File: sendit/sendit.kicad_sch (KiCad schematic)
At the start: 1 part, among them U2 Seeed_Studio_XIAO_ESP32C6

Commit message: big update on the potential design.
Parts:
- removed U2: Seeed_Studio_XIAO_ESP32C6, Seeed Studio XIAO Series Library:XIAO-Generic-Hybrid-14P-2.54-21X17.8MM, symbol yarrboard:Seeed_Studio_XIAO_ESP32C6
- added R3: 10K, Resistor_SMD:R_1206_3216Metric_Pad1.30x1.75mm_HandSolder, symbol Device:R_Small_US
- added U1: ~, yarrboard:Waveshare-ESP32-S3-dev-kit-SMD, symbol yarrboard:ESP32-S3-DevKitC-1
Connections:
- net GND: now also U1.22 (GND), U1.23 (GND), U1.24 (GND), U1.44 (GND)
- net SCL: now also U1.15 (GPIO9)
- net SDA: now also U1.12 (GPIO8)
- new net +3.3V: R3.2, U1.1 (3V3), U1.2 (3V3)
- new net CH1_A0: U1.40 (GPIO2)
- new net CH1_A1: U1.39 (GPIO42)
- new net CH2_A0: U1.38 (GPIO41)
- new net CH2_A1: U1.37 (GPIO40)
- new net CH3_A0: U1.36 (GPIO39)
- new net CH3_A1: U1.34 (GPIO37)
- new net CH4_A0: U1.33 (GPIO36)
- new net CH4_A1: U1.29 (GPIO48)
- new net CH5_A0: U1.28 (GPIO47)
- new net CH5_A1: U1.27 (GPIO21)
- new net CH6_A0: U1.10 (GPIO17)
- new net CH6_A1: U1.9 (GPIO16)
- new net CH7_A0: U1.8 (GPIO15)
- new net CH7_A1: U1.7 (GPIO7)
- new net CH8_A0: U1.6 (GPIO6)
- new net CH8_A1: U1.5 (GPIO5)
- new net CLK: U1.20 (GPIO14)
- new net MISO: U1.19 (GPIO13)
- new net MOSI: U1.18 (GPIO12)
- new net MUX_ENABLE: R3.1, U1.41 (GPIO1)
- new net SD_CS: U1.17 (GPIO11)
- new net SD_DETECT: U1.16 (GPIO10)
- no-connect marks 0 -> 12
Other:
- removed sheet SENDER 1
- removed sheet SENDER 2
- removed sheet SENDER 3
- removed sheet SENDER 4
- removed sheet SENDER 5
- removed sheet SENDER 6
- removed sheet SENDER 7
- removed sheet SENDER 8
- added sheet Analog Channel 1 (analog_channel.kicad_sch)
- added sheet Analog Channel 2 (analog_channel.kicad_sch)
- added sheet Analog Channel 3 (analog_channel.kicad_sch)
- added sheet Analog Channel 4 (analog_channel.kicad_sch)
- added sheet Analog Channel 5 (analog_channel.kicad_sch)
- added sheet Analog Channel 6 (analog_channel.kicad_sch)
- added sheet Analog Channel 7 (analog_channel.kicad_sch)
- added sheet Analog Channel 8 (analog_channel.kicad_sch)
- added sheet MicroSD (microsd.kicad_sch)
- added sheet Power Supply (power_supply.kicad_sch)

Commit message: bigger update
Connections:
- net +5V: now reaches U1.21 (5V0)
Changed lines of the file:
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@@
 (kicad_sch
-	(version 20231120)
+	(version 20250114)
 	(generator "eeschema")
-	(generator_version "8.0")
+	(generator_version "9.0")
 	(paper "A4")
 	(junction
@@
 	(wire
 		(pts
+			(xy 171.45 104.14) (xy 157.48 104.14)
+		)
+		(stroke
+			(width 0)
+			(type default)
+		)
+	)
+	(wire
+		(pts
 			(xy 34.29 54.61) (xy 52.07 54.61)
 		)
@@
 	(wire
 		(pts
+			(xy 157.48 104.14) (xy 157.48 102.87)
+		)
+		(stroke
+			(width 0)
+			(type default)
+		)
+	)
+	(wire
+		(pts
 			(xy 86.36 41.91) (xy 100.33 41.91)
 		)
@@
 	(global_label "SD_DETECT"
 		(shape input)
-		(at 236.22 146.05 180)
+		(at 175.26 149.86 180)
 		(fields_autoplaced yes)
 		(effects
@@
 		)
 		(property "Intersheetrefs" "${INTERSHEET_REFS}"
-			(at 223.0145 146.05 0)
+			(at 162.0545 149.86 0)
 			(effects
 				(font
@@
 	(global_label "MOSI"
 		(shape input)
-		(at 236.22 135.89 180)
+		(at 175.26 139.7 180)
 		(fields_autoplaced yes)
 		(effects
@@
 		)
 		(property "Intersheetrefs" "${INTERSHEET_REFS}"
-			(at 228.6386 135.89 0)
+			(at 167.6786 139.7 0)
 			(effects
 				(font
@@
 	(global_label "CLK"
 		(shape input)
-		(at 236.22 140.97 180)
+		(at 175.26 144.78 180)
 		(fields_autoplaced yes)
 		(effects
@@
 		)
 		(property "Intersheetrefs" "${INTERSHEET_REFS}"
-			(at 229.6667 140.97 0)
+			(at 168.7067 144.78 0)
 			(effects
 				(font
@@
 				)
 				(justify right)
-				(hide yes)
 			)
 		)
@@
 				)
 				(justify right)
-				(hide yes)
 			)
 		)
@@
 	(global_label "SD_CS"
 		(shape input)
-		(at 236.22 133.35 180)
+		(at 175.26 137.16 180)
 		(fields_autoplaced yes)
 		(effects
@@
 		)
 		(property "Intersheetrefs" "${INTERSHEET_REFS}"
-			(at 227.3082 133.35 0)
+			(at 166.3482 137.16 0)
 			(effects
 				(font
@@
 	(global_label "MISO"
 		(shape input)
-		(at 236.22 138.43 180)
+		(at 175.26 142.24 180)
 		(fields_autoplaced yes)
 		(effects
@@
 		)
 		(property "Intersheetrefs" "${INTERSHEET_REFS}"
-			(at 228.6386 138.43 0)
+			(at 167.6786 142.24 0)
 			(effects
 				(font
@@
 	)
 	(symbol
+		(lib_id "power:+5V")
+		(at 157.48 102.87 0)
+		(unit 1)
+		(exclude_from_sim no)
+		(in_bom yes)
+		(on_board yes)
+		(dnp no)
+		(fields_autoplaced yes)
+		(property "Reference" "#PWR0110"
+			(at 157.48 106.68 0)
+			(effects
+				(font
+					(size 1.27 1.27)
+				)
+				(hide yes)
+			)
+		)
+		(property "Value" "+5V"
+			(at 157.48 97.79 0)
+			(effects
+				(font
+					(size 1.27 1.27)
+				)
+			)
+		)
+		(property "Footprint" ""
+			(at 157.48 102.87 0)
+			(effects
+				(font
+					(size 1.27 1.27)
+				)
+				(hide yes)
+			)
+		)
+		(property "Datasheet" ""
+			(at 157.48 102.87 0)
+			(effects
+				(font
+					(size 1.27 1.27)
+				)
+				(hide yes)
+			)
+		)
+		(property "Description" "Power symbol creates a global label with name \"+5V\""
+			(at 157.48 102.87 0)
+			(effects
+				(font
+					(size 1.27 1.27)
+				)
+				(hide yes)
+			)
+		)
+		(pin "1"
+		)
+		(instances
+			(project "sendit"
+				(path "/a355e4d0-2918-44fc-be8d-2503b84c6d6c"
+					(reference "#PWR0110")
+					(unit 1)
+				)
+			)
+		)
+	)
+	(symbol
 		(lib_id "power:GND")
 		(at 189.23 116.84 0)
@@
 		(at 52.07 67.31)
 		(size 34.29 10.16)
+		(exclude_from_sim no)
+		(in_bom yes)
+		(on_board yes)
+		(dnp no)
 		(fields_autoplaced yes)
 		(stroke
@@
 	)
 	(sheet
-		(at 176.53 134.62)
-		(size 33.02 11.43)
+		(at 41.91 177.8)
+		(size 33.02 3.81)
+		(exclude_from_sim no)
+		(in_bom yes)
+		(on_board yes)
+		(dnp no)
 		(fields_autoplaced yes)
 		(stroke
@@
 		)
 		(property "Sheetname" "Power Supply"
-			(at 176.53 133.9084 0)
+			(at 41.91 177.0884 0)
 			(effects
 				(font
@@
 		)
 		(property "Sheetfile" "power_supply.kicad_sch"
-			(at 176.53 146.6346 0)
+			(at 41.91 182.1946 0)
 			(effects
 				(font
@@
 		(at 107.95 119.38)
 		(size 21.59 15.24)
+		(exclude_from_sim no)
+		(in_bom yes)
+		(on_board yes)
+		(dnp no)
 		(fields_autoplaced yes)
 		(stroke
@@
 		(at 52.07 99.06)
 		(size 34.29 10.16)
+		(exclude_from_sim no)
+		(in_bom yes)
+		(on_board yes)
+		(dnp no)
 		(fields_autoplaced yes)
 		(stroke
@@
 		(at 52.07 129.54)
 		(size 34.29 10.16)
+		(exclude_from_sim no)
+		(in_bom yes)
+		(on_board yes)
+		(dnp no)
 		(fields_autoplaced yes)
 		(stroke
@@
 		(at 52.07 52.07)
 		(size 34.29 10.16)
+		(exclude_from_sim no)
+		(in_bom yes)
+		(on_board yes)
+		(dnp no)
 		(fields_autoplaced yes)
 		(stroke
@@
 		(at 52.07 144.78)
 		(size 34.29 10.16)
+		(exclude_from_sim no)
+		(in_bom yes)
+		(on_board yes)
+		(dnp no)
 		(fields_autoplaced yes)
 		(stroke
@@
 	)
 	(sheet
-		(at 236.22 130.81)
+		(at 175.26 134.62)
 		(size 30.48 17.78)
+		(exclude_from_sim no)
+		(in_bom yes)
+		(on_board yes)
+		(dnp no)
 		(fields_autoplaced yes)
 		(stroke
@@
 		)
 		(property "Sheetname" "MicroSD"
-			(at 236.22 130.0984 0)
+			(at 175.26 133.9084 0)
 			(effects
 				(font
@@
 		)
 		(property "Sheetfile" "microsd.kicad_sch"
-			(at 236.22 149.1746 0)
+			(at 175.26 152.9846 0)
 			(effects
 				(font
@@
 		)
 		(pin "MOSI" input
-			(at 236.22 135.89 180)
+			(at 175.26 139.7 180)
 			(effects
 				(font
@@
 		)
 		(pin "CS" input
-			(at 236.22 133.35 180)
+			(at 175.26 137.16 180)
 			(effects
 				(font
@@
 		)
 		(pin "CLK" input
-			(at 236.22 140.97 180)
+			(at 175.26 144.78 180)
 			(effects
 				(font
@@
 		)
 		(pin "MISO" input
-			(at 236.22 138.43 180)
+			(at 175.26 142.24 180)
 			(effects
 				(font
@@
 		)
 		(pin "DETECT" input
-			(at 236.22 146.05 180)
+			(at 175.26 149.86 180)
 			(effects
 				(font
@@
 		(at 107.95 57.15)
 		(size 21.59 15.24)
+		(exclude_from_sim no)
+		(in_bom yes)
+		(on_board yes)
+		(dnp no)
 		(fields_autoplaced yes)
 		(stroke
@@
 		(at 52.07 36.83)
 		(size 34.29 10.16)
+		(exclude_from_sim no)
+		(in_bom yes)
+		(on_board yes)
+		(dnp no)
 		(fields_autoplaced yes)
 		(stroke
@@
 		(at 52.07 82.55)
 		(size 34.29 10.16)
+		(exclude_from_sim no)
+		(in_bom yes)
+		(on_board yes)
+		(dnp no)
 		(fields_autoplaced yes)
 		(stroke
@@
 		(at 52.07 114.3)
 		(size 34.29 10.16)
+		(exclude_from_sim no)
+		(in_bom yes)
+		(on_board yes)
+		(dnp no)
 		(fields_autoplaced yes)
 		(stroke
@@
 		)
 	)
+	(embedded_fonts no)
 )

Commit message: changed from mux to pin jumpers
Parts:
- removed R3: 10K, Resistor_SMD:R_1206_3216Metric_Pad1.30x1.75mm_HandSolder, symbol Device:R_Small_US
- added H10, H11, H12, H13: MountingHole_Pad, MountingHole:MountingHole_3.2mm_M3_ISO14580_Pad, symbol Mechanical:MountingHole_Pad
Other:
- sheet Analog Channel 1 ports: added none; removed A0, A1, EN
- sheet Analog Channel 2 ports: added none; removed A0, A1, EN
- sheet Analog Channel 3 ports: added none; removed A0, A1, EN
- sheet Analog Channel 4 ports: added none; removed A0, A1, EN
- sheet Analog Channel 5 ports: added none; removed A0, A1, EN
- sheet Analog Channel 6 ports: added none; removed A0, A1, EN
- sheet Analog Channel 7 ports: added none; removed A0, A1, EN
- sheet Analog Channel 8 ports: added none; removed A0, A1, EN

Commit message: layout work.
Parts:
- renumbered H10 to H1, H11 to H2, H12 to H3, H13 to H4
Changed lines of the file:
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@@
 		(dnp no)
 		(fields_autoplaced yes)
-		(property "Reference" "H13"
+		(property "Reference" "H4"
 			(at 153.67 190.4999 0)
 			(effects
@@
 			(project "sendit"
 				(path "/a355e4d0-2918-44fc-be8d-2503b84c6d6c"
-					(reference "H13")
+					(reference "H4")
 					(unit 1)
 				)
@@
 		(on_board yes)
 		(dnp no)
-		(property "Reference" "#PWR0108"
+		(property "Reference" "#PWR06"
 			(at 214.63 59.69 0)
 			(effects
@@
 			(project "sendit"
 				(path "/a355e4d0-2918-44fc-be8d-2503b84c6d6c"
-					(reference "#PWR0108")
+					(reference "#PWR06")
 					(unit 1)
 				)
@@
 		(dnp no)
 		(fields_autoplaced yes)
-		(property "Reference" "#PWR0109"
+		(property "Reference" "#PWR02"
 			(at 133.35 133.35 0)
 			(effects
@@
 			(project "sendit"
 				(path "/a355e4d0-2918-44fc-be8d-2503b84c6d6c"
-					(reference "#PWR0109")
+					(reference "#PWR02")
 					(unit 1)
 				)
@@
 		(dnp no)
 		(fields_autoplaced yes)
-		(property "Reference" "H10"
+		(property "Reference" "H1"
 			(at 128.27 182.8799 0)
 			(effects
@@
 			(project "sendit"
 				(path "/a355e4d0-2918-44fc-be8d-2503b84c6d6c"
-					(reference "H10")
+					(reference "H1")
 					(unit 1)
 				)
@@
 		(dnp no)
 		(fields_autoplaced yes)
-		(property "Reference" "#PWR0110"
+		(property "Reference" "#PWR03"
 			(at 157.48 106.68 0)
 			(effects
@@
 			(project "sendit"
 				(path "/a355e4d0-2918-44fc-be8d-2503b84c6d6c"
-					(reference "#PWR0110")
+					(reference "#PWR03")
 					(unit 1)
 				)
@@
 		(dnp no)
 		(fields_autoplaced yes)
-		(property "Reference" "#PWR0107"
+		(property "Reference" "#PWR05"
 			(at 189.23 123.19 0)
 			(effects
@@
 			(project "sendit"
 				(path "/a355e4d0-2918-44fc-be8d-2503b84c6d6c"
-					(reference "#PWR0107")
+					(reference "#PWR05")
 					(unit 1)
 				)
@@
 		(dnp no)
 		(fields_autoplaced yes)
-		(property "Reference" "H12"
+		(property "Reference" "H3"
 			(at 153.67 182.8799 0)
 			(effects
@@
 			(project "sendit"
 				(path "/a355e4d0-2918-44fc-be8d-2503b84c6d6c"
-					(reference "H12")
+					(reference "H3")
 					(unit 1)
 				)
@@
 		(dnp no)
 		(fields_autoplaced yes)
-		(property "Reference" "#PWR0106"
+		(property "Reference" "#PWR04"
 			(at 163.83 50.8 0)
 			(effects
@@
 			(project "sendit"
 				(path "/a355e4d0-2918-44fc-be8d-2503b84c6d6c"
-					(reference "#PWR0106")
+					(reference "#PWR04")
 					(unit 1)
 				)
@@
 		(dnp no)
 		(fields_autoplaced yes)
-		(property "Reference" "H11"
+		(property "Reference" "H2"
 			(at 128.27 190.4999 0)
 			(effects
@@
 			(project "sendit"
 				(path "/a355e4d0-2918-44fc-be8d-2503b84c6d6c"
-					(reference "H11")
-					(unit 1)
-				)
+					(reference "H2")
+					(unit 1)
+				)

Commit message: first pass layout finished.
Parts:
- added R77, R78: 4.7k, Resistor_SMD:R_0603_1608Metric, symbol Device:R_Small_US
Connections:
- net +3.3V: now also R77.2, R78.2
- net GND: now also H1.1, H2.1, H3.1, H4.1
- net SCL: now also R78.1
- net SDA: now also R77.1
- net CH1_A0: no longer names the net of U1.40 (GPIO2)
- net CH1_A1: no longer names the net of U1.39 (GPIO42)
- net CH2_A0: no longer names the net of U1.38 (GPIO41)
- net CH2_A1: no longer names the net of U1.37 (GPIO40)
- net CH3_A0: no longer names the net of U1.36 (GPIO39)
- net CH3_A1: no longer names the net of U1.34 (GPIO37)
- net CH4_A0: no longer names the net of U1.33 (GPIO36)
- net CH4_A1: no longer names the net of U1.29 (GPIO48)
- net CH5_A0: no longer names the net of U1.28 (GPIO47)
- net CH5_A1: no longer names the net of U1.27 (GPIO21)
- net CH6_A0: no longer names the net of U1.10 (GPIO17)
- net CH6_A1: no longer names the net of U1.9 (GPIO16)
- net CH7_A0: no longer names the net of U1.8 (GPIO15)
- net CH7_A1: no longer names the net of U1.7 (GPIO7)
- net CH8_A0: no longer names the net of U1.6 (GPIO6)
- net CH8_A1: no longer names the net of U1.5 (GPIO5)
- net MUX_ENABLE: no longer names the net of U1.41 (GPIO1)
- no-connect marks 12 -> 30
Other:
- moved on the sheet: H1, H2, H3, H4

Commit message: finished layout and routing
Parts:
- added LOGO1: ~, yarrboard:Logo Small, symbol yarrboard:Yarrboard
- added LOGO2: Logo_Open_Hardware_Small, Symbol:OSHW-Logo_5.7x6mm_SilkScreen, symbol Graphic:Logo_Open_Hardware_Small
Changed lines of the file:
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@@
+	)
+	(symbol
+		(lib_id "yarrboard:Yarrboard")
+		(at 107.95 175.26 0)
+		(unit 1)
+		(exclude_from_sim no)
+		(in_bom no)
+		(on_board yes)
+		(dnp no)
+		(fields_autoplaced yes)
+		(property "Reference" "LOGO1"
+			(at 107.95 171.45 0)
+			(effects
+				(font
+					(size 1.27 1.27)
+				)
+			)
+		)
+		(property "Value" "~"
+			(at 107.95 173.99 0)
+			(effects
+				(font
+					(size 1.27 1.27)
+				)
+				(hide yes)
+			)
+		)
+		(property "Footprint" "yarrboard:Logo Small"
+			(at 107.95 175.26 0)
+			(effects
+				(font
+					(size 1.27 1.27)
+				)
+				(hide yes)
+			)
+		)
+		(property "Datasheet" ""
+			(at 107.95 175.26 0)
+			(effects
+				(font
+					(size 1.27 1.27)
+				)
+				(hide yes)
+			)
+		)
+		(property "Description" ""
+			(at 107.95 175.26 0)
+			(effects
+				(font
+					(size 1.27 1.27)
+				)
+				(hide yes)
+			)
+		)
+		(instances
+			(project ""
+				(path "/a355e4d0-2918-44fc-be8d-2503b84c6d6c"
+					(reference "LOGO1")
+					(unit 1)
+				)
+			)
+		)
 	)
 	(symbol
@@
 					(unit 1)
 				)
+			)
+		)
+	)
+	(symbol
+		(lib_id "Graphic:Logo_Open_Hardware_Small")
+		(at 107.95 189.23 0)
+		(unit 1)
+		(exclude_from_sim yes)
+		(in_bom no)
+		(on_board no)
+		(dnp no)
+		(fields_autoplaced yes)
+		(property "Reference" "LOGO2"
+			(at 107.95 182.245 0)
+			(effects
+				(font
+					(size 1.27 1.27)
+				)
+				(hide yes)
+			)
+		)
+		(property "Value" "Logo_Open_Hardware_Small"
+			(at 107.95 194.945 0)
+			(effects
+				(font
+					(size 1.27 1.27)
+				)
+				(hide yes)
+			)
+		)
+		(property "Footprint" "Symbol:OSHW-Logo_5.7x6mm_SilkScreen"
+			(at 107.95 189.23 0)
+			(effects
+				(font
+					(size 1.27 1.27)
+				)
+				(hide yes)
+			)
+		)
+		(property "Datasheet" "~"
+			(at 107.95 189.23 0)
+			(effects
+				(font
+					(size 1.27 1.27)
+				)
+				(hide yes)
+			)
+		)
+		(property "Description" "Open Hardware logo, small"
+			(at 107.95 189.23 0)
+			(effects
+				(font
+					(size 1.27 1.27)
+				)
+				(hide yes)
+			)
+		)
+		(instances
+			(project ""
+				(path "/a355e4d0-2918-44fc-be8d-2503b84c6d6c"
+					(reference "LOGO2")
+					(unit 1)
+				)

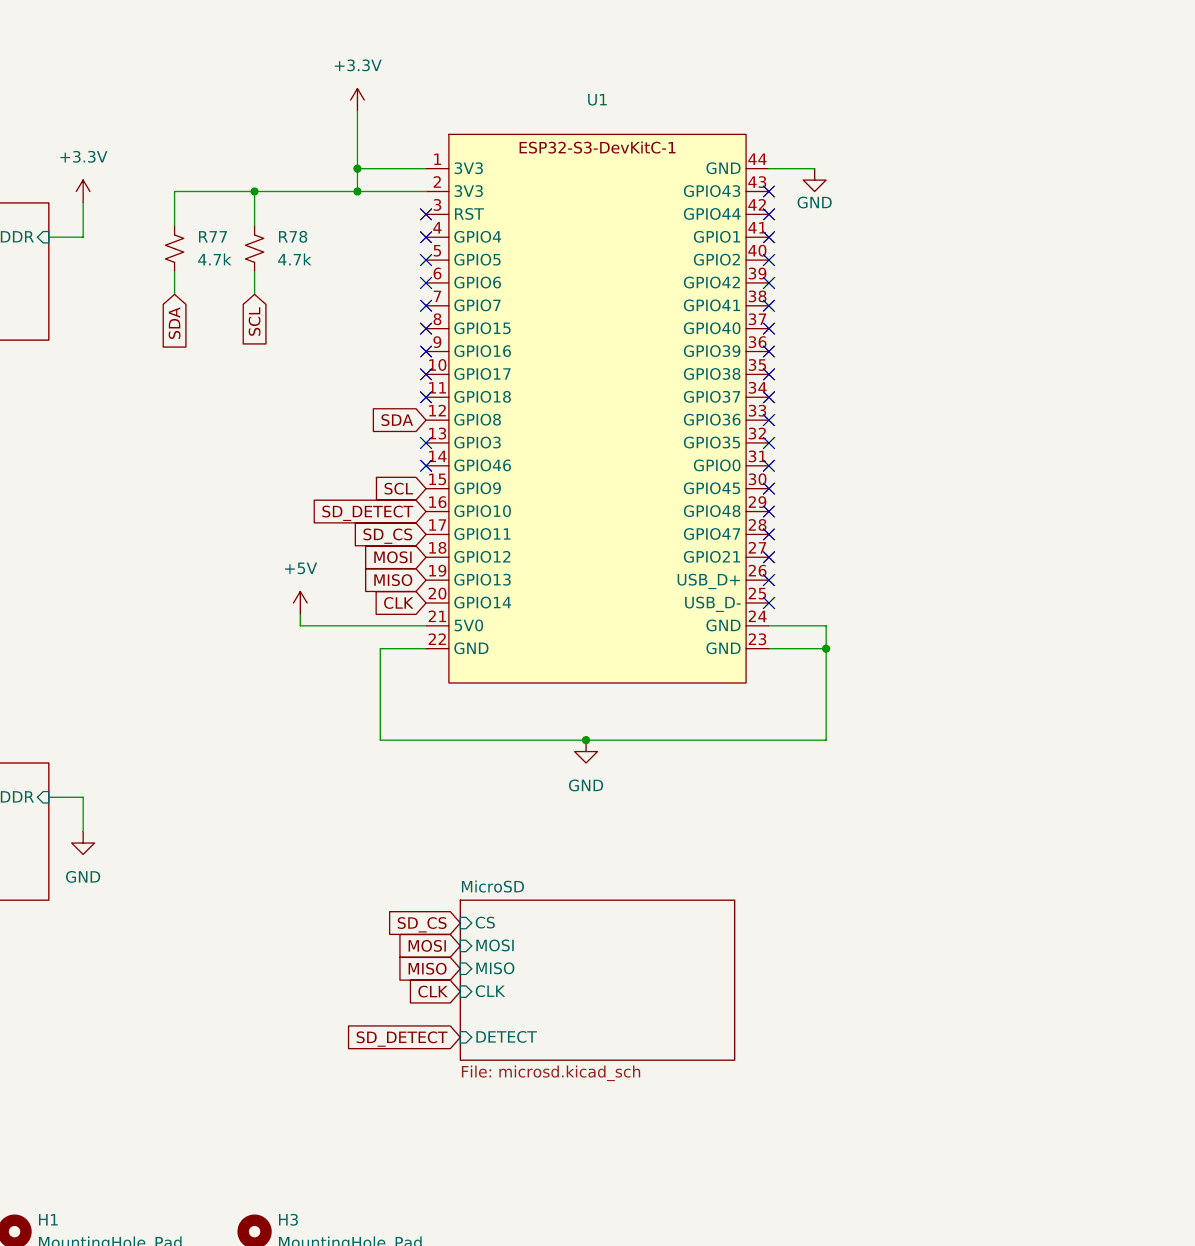
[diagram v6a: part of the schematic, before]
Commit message: added fuses, 24v filters, and indicator leds.
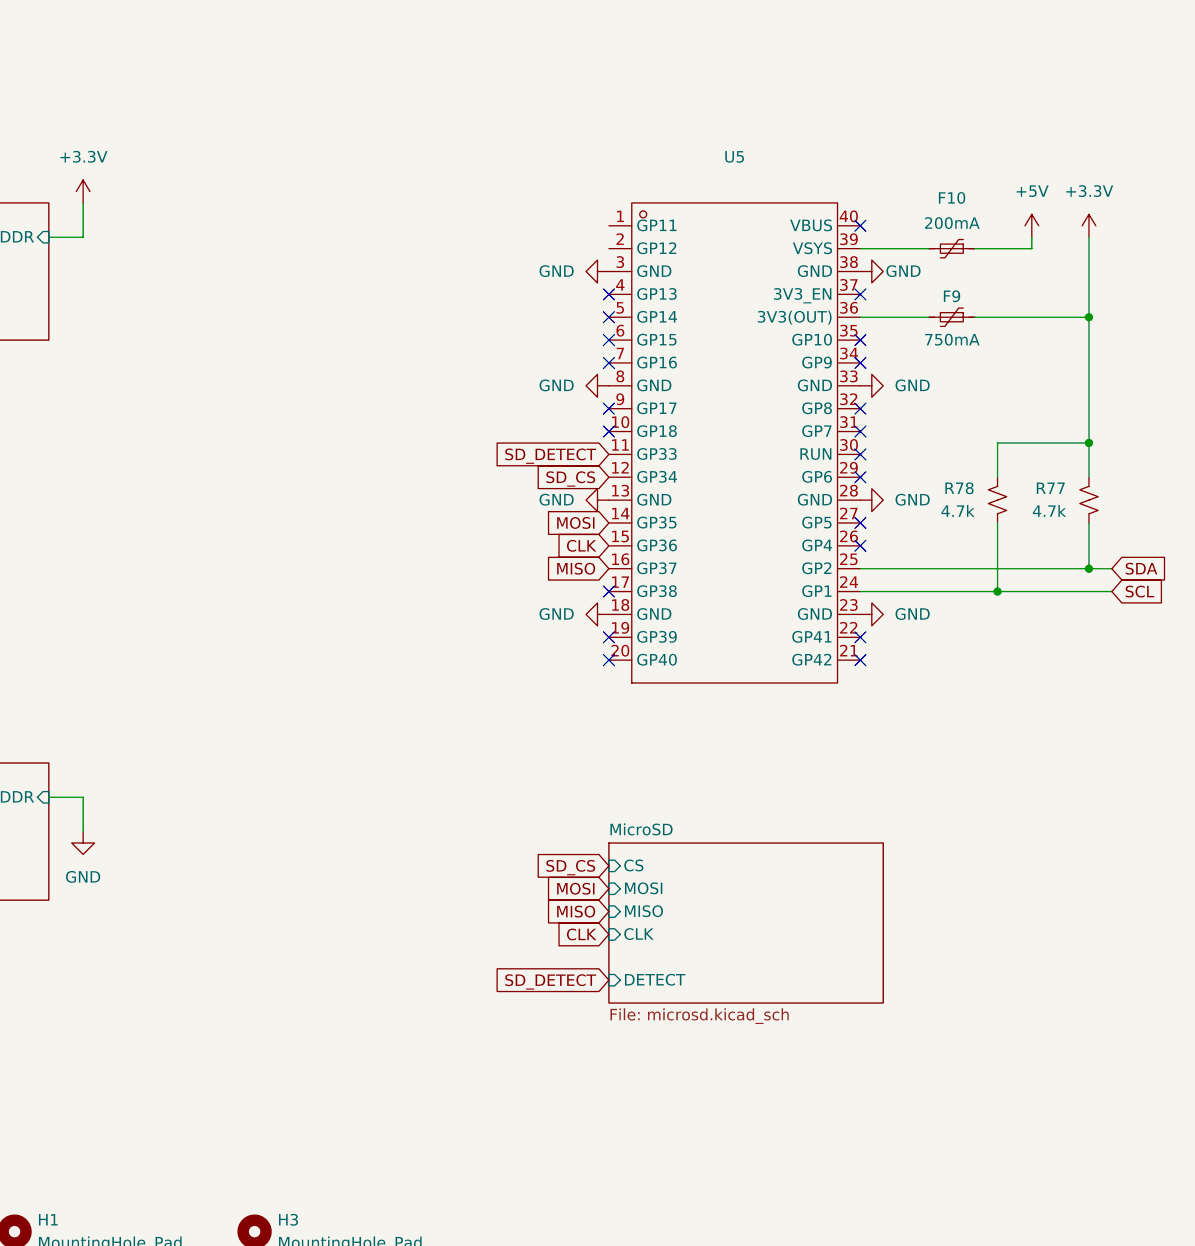
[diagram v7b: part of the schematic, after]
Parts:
- removed U1: ~, yarrboard:Waveshare-ESP32-S3-dev-kit-SMD, symbol yarrboard:ESP32-S3-DevKitC-1
- added F10: 200mA, Fuse:Fuse_0805_2012Metric, symbol Device:Polyfuse_Small
- added F9: 750mA, Fuse:Fuse_0805_2012Metric, symbol Device:Polyfuse_Small
- added U5: ~, yarrboard:ESP32-S3-PICO, symbol yarrboard:ESP32-S3-PICO
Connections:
- net +3.3V: now also F9.1
- net +5V: now also F10.1
- net CLK: now also U5.15 (GP36)
- net GND: now also U5.13 (GND), U5.18 (GND), U5.23 (GND), U5.28 (GND), U5.3 (GND), U5.33 (GND), U5.38 (GND), U5.8 (GND)
- net MISO: now also U5.16 (GP37)
- net MOSI: now also U5.14 (GP35)
- net SCL: now also U5.24 (GP1)
- net SDA: now also U5.25 (GP2)
- net SD_CS: now also U5.12 (GP34)
- net SD_DETECT: now also U5.11 (GP33)
- new net: F9.2, U5.36 (3V3(OUT))
- new net: F10.2, U5.39 (VSYS)
- no-connect marks 30 -> 21
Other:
- moved on the sheet: R77, R78
